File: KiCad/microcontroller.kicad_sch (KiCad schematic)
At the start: 46 parts, among them J1 Debugger, SW1 Reset switch, U1 STM32F051C6Tx, U7 24LC256

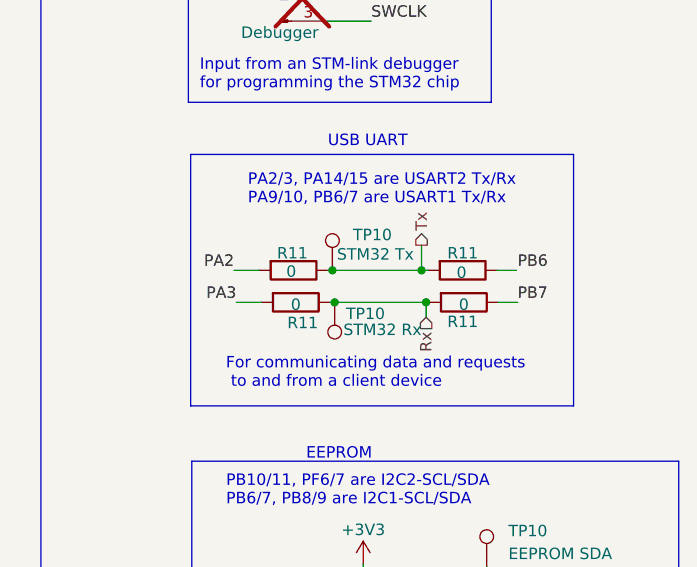
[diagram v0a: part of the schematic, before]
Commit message: updated 0Ω to be DNP
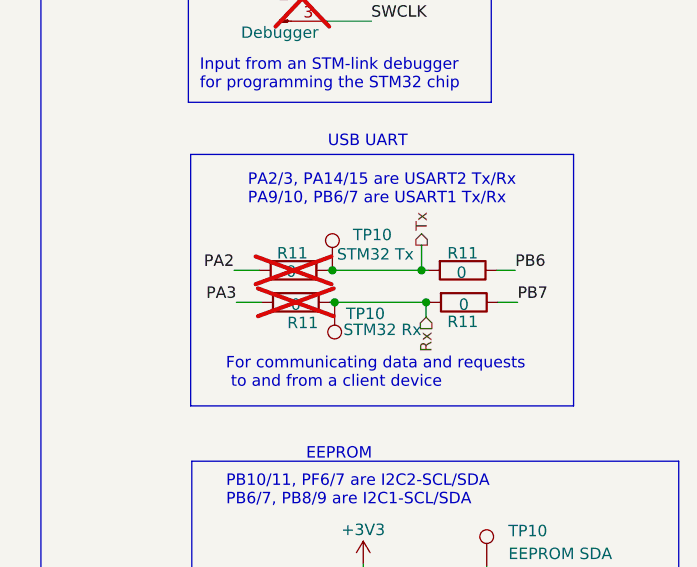
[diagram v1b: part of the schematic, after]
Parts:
- R11: now not fitted
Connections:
- net PB6: now also R11.1
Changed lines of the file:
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@@
-    (stroke (width 0) (type default))
-  )
-  (wire (pts (xy 262.89 64.516) (xy 265.049 64.516))
     (stroke (width 0) (type default))
   )
@@
   )
   (wire (pts (xy 59.69 128.778) (xy 60.96 128.778))
+    (stroke (width 0) (type default))
+  )
+  (wire (pts (xy 262.89 64.516) (xy 264.922 64.516))
     (stroke (width 0) (type default))
   )
@@
     (effects (font (size 1.27 1.27)) (justify left bottom))
   )
-  (label "PB6" (at 265.176 64.516 0) (fields_autoplaced)
+  (label "PB6" (at 264.922 64.516 0) (fields_autoplaced)
     (effects (font (size 1.27 1.27)) (justify left bottom))
   )
@@
   )
   (symbol (lib_id "Device:R") (at 240.284 64.516 270) (unit 1)
-    (in_bom yes) (on_board yes) (dnp no)
+    (in_bom yes) (on_board yes) (dnp yes)
     (property "Reference" "R11" (at 240.157 62.611 90)
       (effects (font (size 1.27 1.27)))
@@
   )
   (symbol (lib_id "Device:R") (at 240.538 68.072 270) (unit 1)
-    (in_bom yes) (on_board yes) (dnp no)
+    (in_bom yes) (on_board yes) (dnp yes)
     (property "Reference" "R11" (at 241.3 70.358 90)
       (effects (font (size 1.27 1.27)))

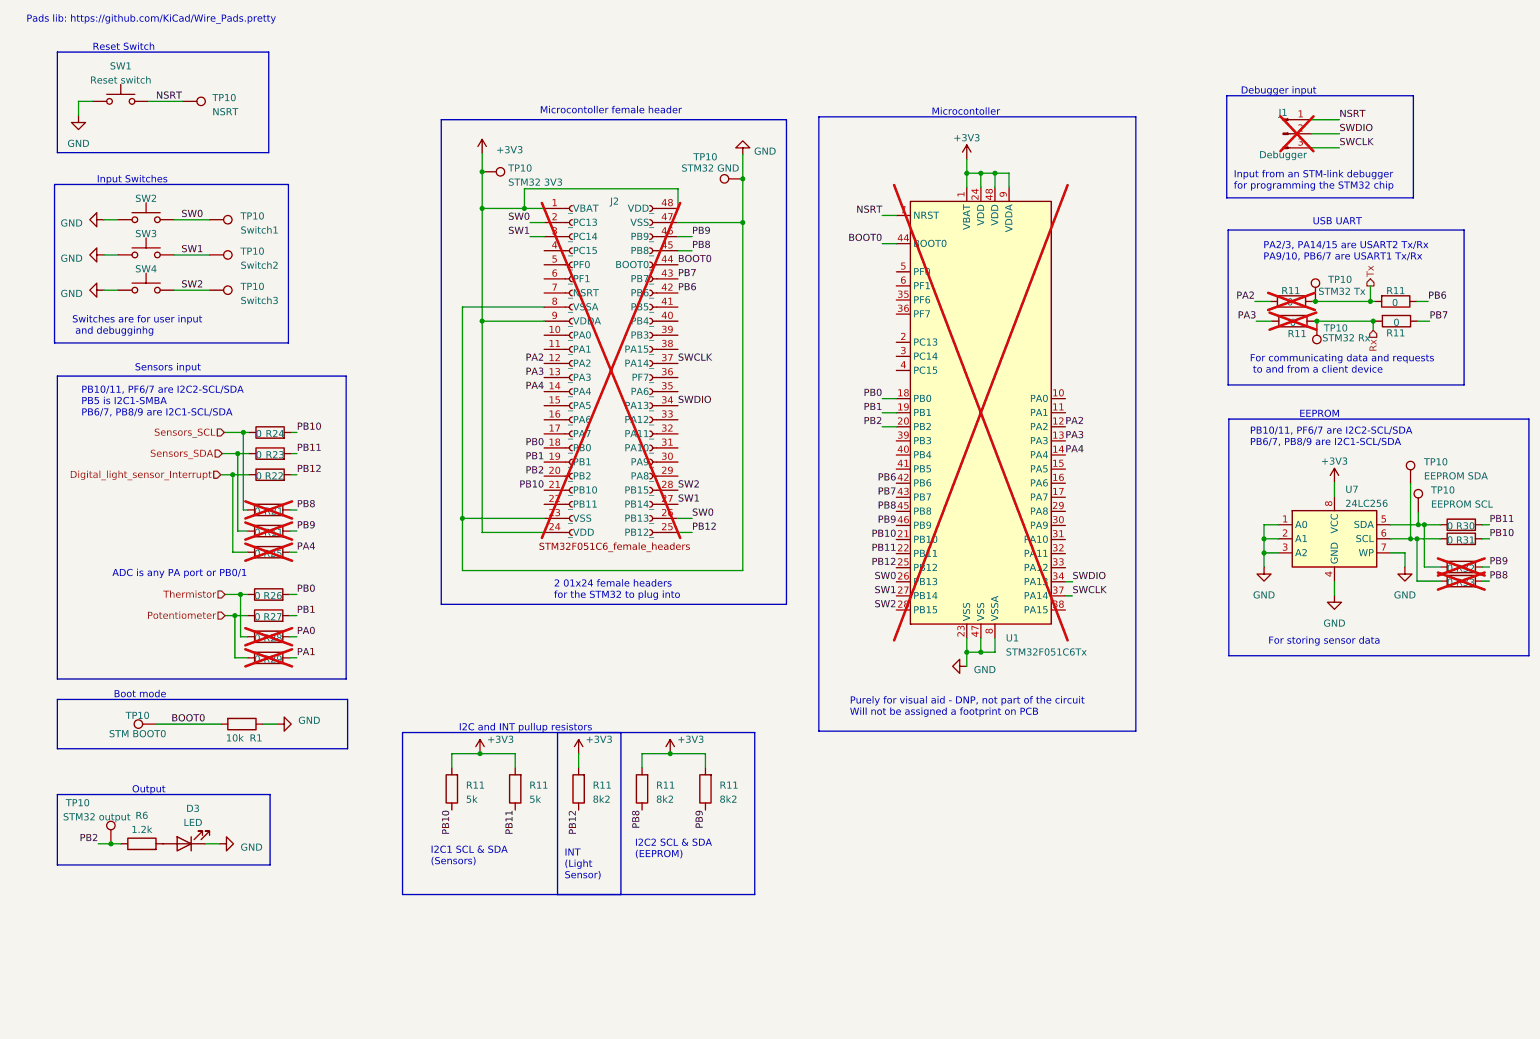
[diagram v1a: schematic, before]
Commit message: changed a bunch of net labels, changed some uc schem stuff
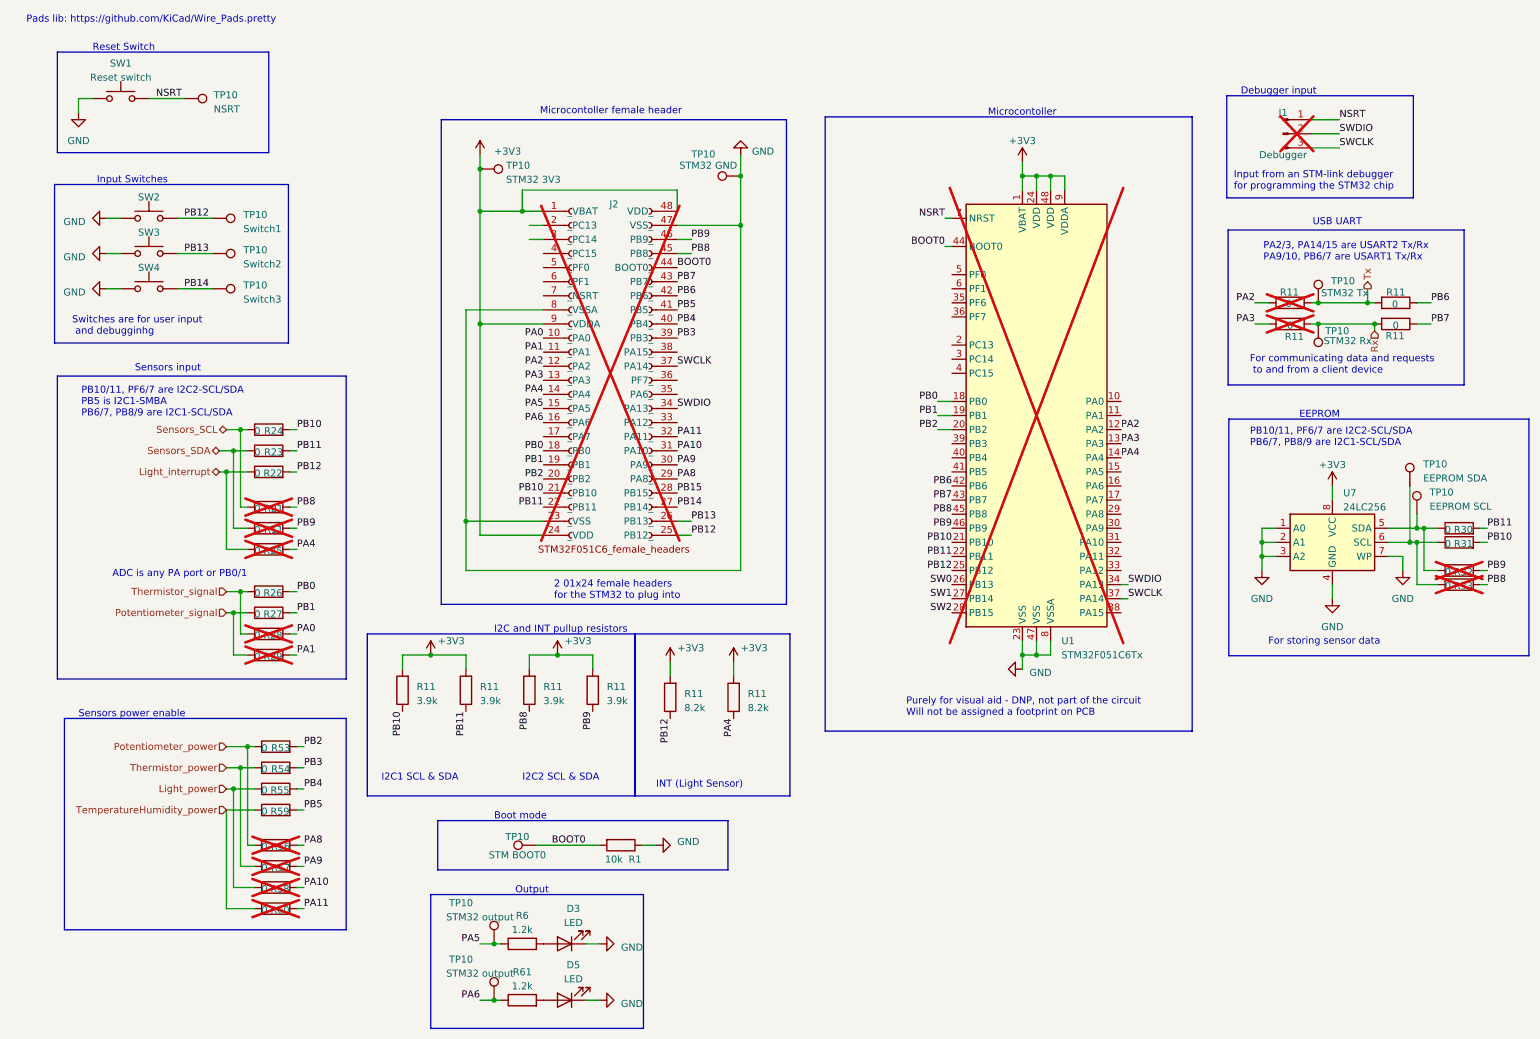
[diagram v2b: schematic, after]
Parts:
- added D5: LED, symbol Device:LED
- added R11: 8.2k, symbol Device:R
- added R53, R54, R55, R56, R57, R58, R59, R60: 0, symbol Device:R
- added R61: 1.2k, symbol Device:R
- added TP10: STM32 output, symbol Connector:TestPoint
- R11: value 5k -> 3.9k
- R11: value 8k2 -> 3.9k
- R11: value 8k2 -> 8.2k
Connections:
- net +3V3: now also R11.2
- net GND: now also D5.1 (K)
- net PA0: now also J2.10 (_PA0)
- net PA1: now also J2.11 (_PA1)
- net PA4: now also R11.1
- net PB11: now also J2.22 (_PB11)
- net PB12: now also SW2.2, TP10.1
- net PB2: now also R53.2; no longer R6.1, TP10.1
- net SW0: no longer J2.2 (_PC13), J2.26 (PB13_), SW2.2, TP10.1
- net SW1: no longer J2.27 (PB14_), J2.3 (_PC14), SW3.2, TP10.1
- net SW2: no longer J2.28 (PB15_), SW4.2, TP10.1
- net PA5: now reaches J2.15 (_PA5)
- net PA5: now also R6.1, TP10.1
- net PA6: now reaches J2.16 (_PA6)
- net PA6: now also R61.1, TP10.1
- net PA8: now reaches J2.29 (PA8_)
- net PA8: now also R56.2
- net PA9: now reaches J2.30 (PA9_)
- net PA9: now also R57.2
- net PA10: now reaches J2.31 (PA10_)
- net PA10: now also R58.2
- net PA11: now reaches J2.32 (PA11_)
- net PA11: now also R60.2
- net PB3: now reaches J2.39 (PB3_)
- net PB3: now also R54.2
- net PB4: now reaches J2.40 (PB4_)
- net PB4: now also R55.2
- net PB5: now reaches J2.41 (PB5_)
- net PB5: now also R59.2
- net Digital_light_sensor_Interrupt renamed Light_interrupt
- net Potentiometer renamed Potentiometer_signal
- net Thermistor renamed Thermistor_signal
- new net: D5.2 (A), R61.2
- new net Light_power: R55.1, R58.1
- new net PB13: J2.26 (PB13_), SW3.2, TP10.1
- new net PB14: J2.27 (PB14_), SW4.2, TP10.1
- new net PB15: J2.28 (PB15_)
- new net Potentiometer_power: R53.1, R56.1
- new net TemperatureHumidity_power: R59.1, R60.1
- new net Thermistor_power: R54.1, R57.1
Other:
- note added: "I2C1 SCL & SDA"
- note added: "I2C2 SCL & SDA"
- note added: "Sensors power enable"
- note removed: "I2C1 SCL & SDA (Sensors)"
- note removed: "I2C2 SCL & SDA (EEPROM)"
- moved on the sheet: D3, J2, R1, R11, R21, R22, R23, R24, R25, R26, R27, R28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

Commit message: updated net labelling scheme on schematic, changed some port connections on microcontroller
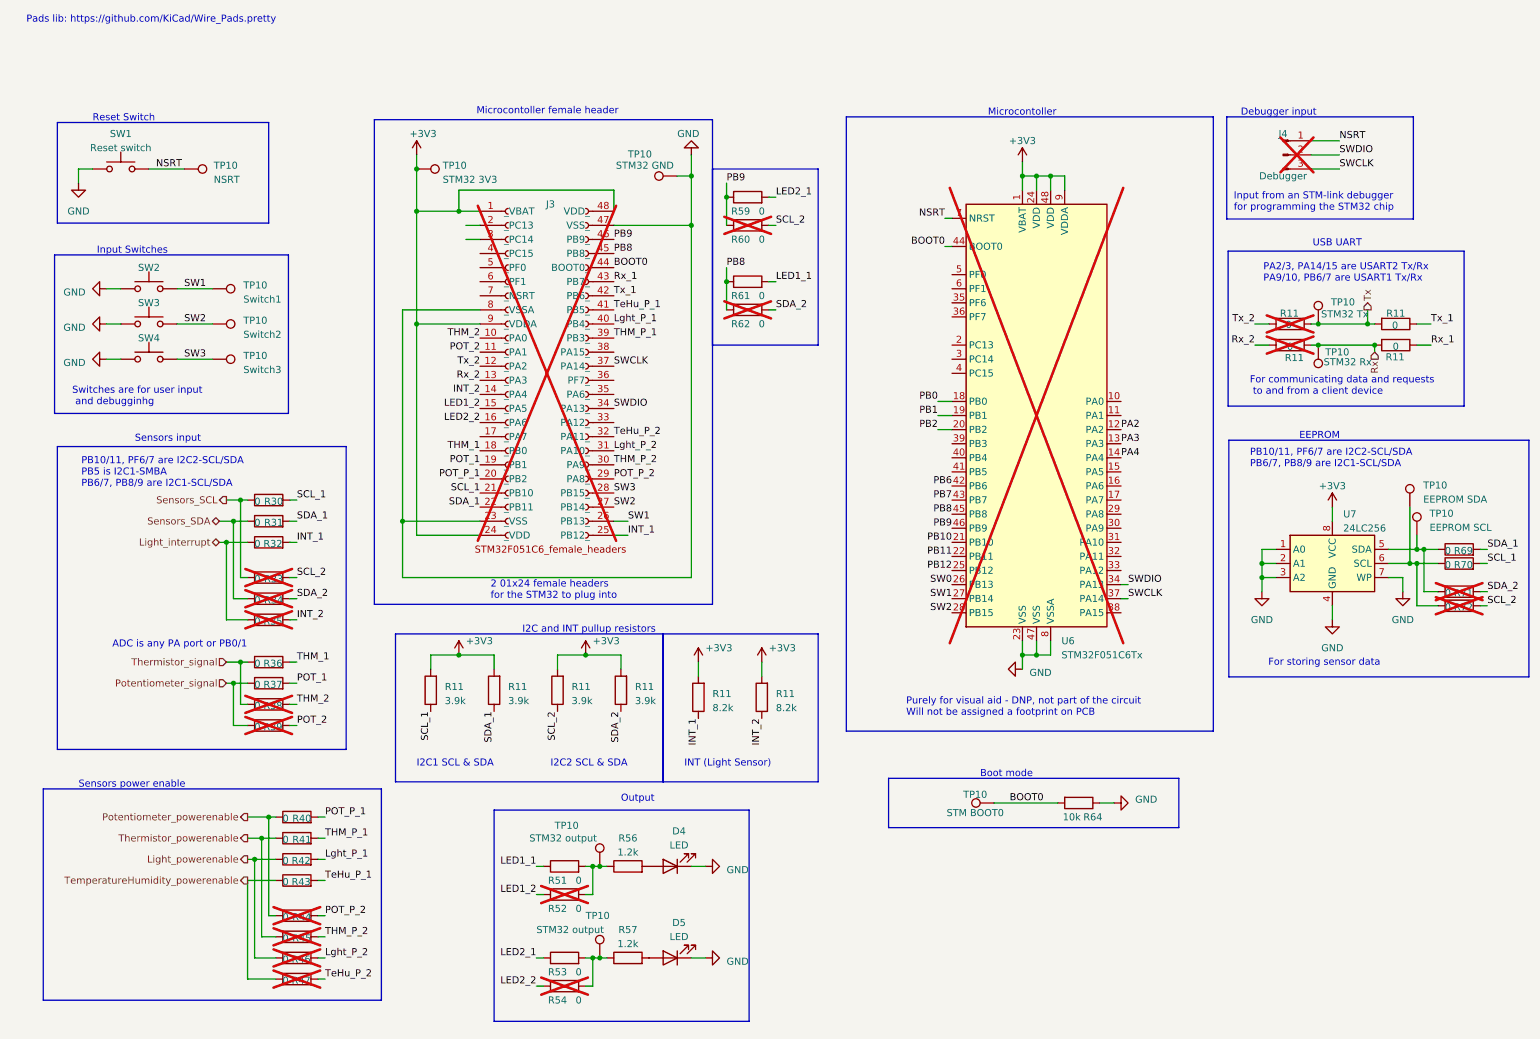
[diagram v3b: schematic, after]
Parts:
- added R51, R52, R53, R54, R59, R60, R61, R62: 0, symbol Device:R
- renumbered D3 to D4, J2 to J3, J1 to J4, R24 to R30, R23 to R31, R22 to R32, R21 to R33, R11 to R34, R25 to R35, R26 to R36, R27 to R37, R28 to R38, R29 to R39, R53 to R40, R54 to R41, R55 to R42, R59 to R43, R56 to R44, R57 to R45, R58 to R46, R60 to R47, R6 to R56, R61 to R57, R1 to R64, R30 to R69, R31 to R70, R32 to R71, R33 to R72, U1 to U6
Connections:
- net PB15 is gone; now on net SW3: J3.28 (PB15_)
- net PA2: no longer J3.12 (_PA2), R11.2
- net PA3: no longer J3.13 (_PA3), R11.2
- net PA4: no longer J3.14 (_PA4), R11.1, R35.2
- net PB0: no longer J3.18 (_PB0), R36.2
- net PB1: no longer J3.19 (_PB1), R37.2
- net PB10: no longer J3.21 (_PB10), R11.1, R30.2, R70.2
- net PB11: no longer J3.22 (_PB11), R11.1, R31.2, R69.2
- net PB12: no longer J3.25 (PB12_), R11.1, R32.2, SW2.2, TP10.1
- net PB2: no longer J3.20 (_PB2), R40.2
- net PB6: no longer J3.42 (PB6_), R11.1
- net PB7: no longer J3.43 (PB7_), R11.1
- net PB8: now also R61.1, R62.1; no longer R11.1, R33.2, R72.2
- net PB9: now also R59.1, R60.1; no longer R11.1, R34.2, R71.2
- net SW1: now also J3.26 (PB13_), SW2.2, TP10.1
- net SW2: now also J3.27 (PB14_), SW3.2, TP10.1
- net Light_power renamed Light_powerenable
- net PA0 renamed THM_2
- net PA1 renamed POT_2
- net PA10 renamed Lght_P_2
- net PA11 renamed TeHu_P_2
- net PA5: no longer names the net of R56.1, TP10.1
- net PA5: now also R51.2, R52.2; no longer J3.15 (_PA5)
- net PA6: no longer names the net of R57.1, TP10.1
- net PA6: now also R53.2, R54.2; no longer J3.16 (_PA6)
- net PA8 renamed POT_P_2
- net PA9 renamed THM_P_2
- removed net PB13: J3.26 (PB13_), SW3.2, TP10.1
- net PB14 renamed SW3
- net SW3: no longer J3.27 (PB14_)
- net PB3 renamed THM_P_1
- net PB4 renamed Lght_P_1
- net PB5 renamed TeHu_P_1
- net Potentiometer_power renamed Potentiometer_powerenable
- net TemperatureHumidity_power renamed TemperatureHumidity_powerenable
- net Thermistor_power renamed Thermistor_powerenable
- new net INT_1: J3.25 (PB12_), R11.1, R32.2
- new net INT_2: J3.14 (_PA4), R11.1, R35.2
- new net LED1_1: R51.1, R61.2
- new net LED1_2: J3.15 (_PA5), R52.1
- new net LED2_1: R53.1, R59.2
- new net LED2_2: J3.16 (_PA6), R54.1
- new net POT_1: J3.19 (_PB1), R37.2
- new net POT_P_1: J3.20 (_PB2), R40.2
- new net Rx_1: J3.43 (PB7_), R11.1
- new net Rx_2: J3.13 (_PA3), R11.2
- new net SCL_1: J3.21 (_PB10), R11.1, R30.2, R70.2
- new net SCL_2: R11.1, R33.2, R60.2, R72.2
- new net SDA_1: J3.22 (_PB11), R11.1, R31.2, R69.2
- new net SDA_2: R11.1, R34.2, R62.2, R71.2
- new net THM_1: J3.18 (_PB0), R36.2
- new net Tx_1: J3.42 (PB6_), R11.1
- new net Tx_2: J3.12 (_PA2), R11.2
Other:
- moved on the sheet: D4, D5, J3, J4, R11, R30, R31, R32, R33, R34, R35, R36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

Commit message: ran ERCs and fixed the errors
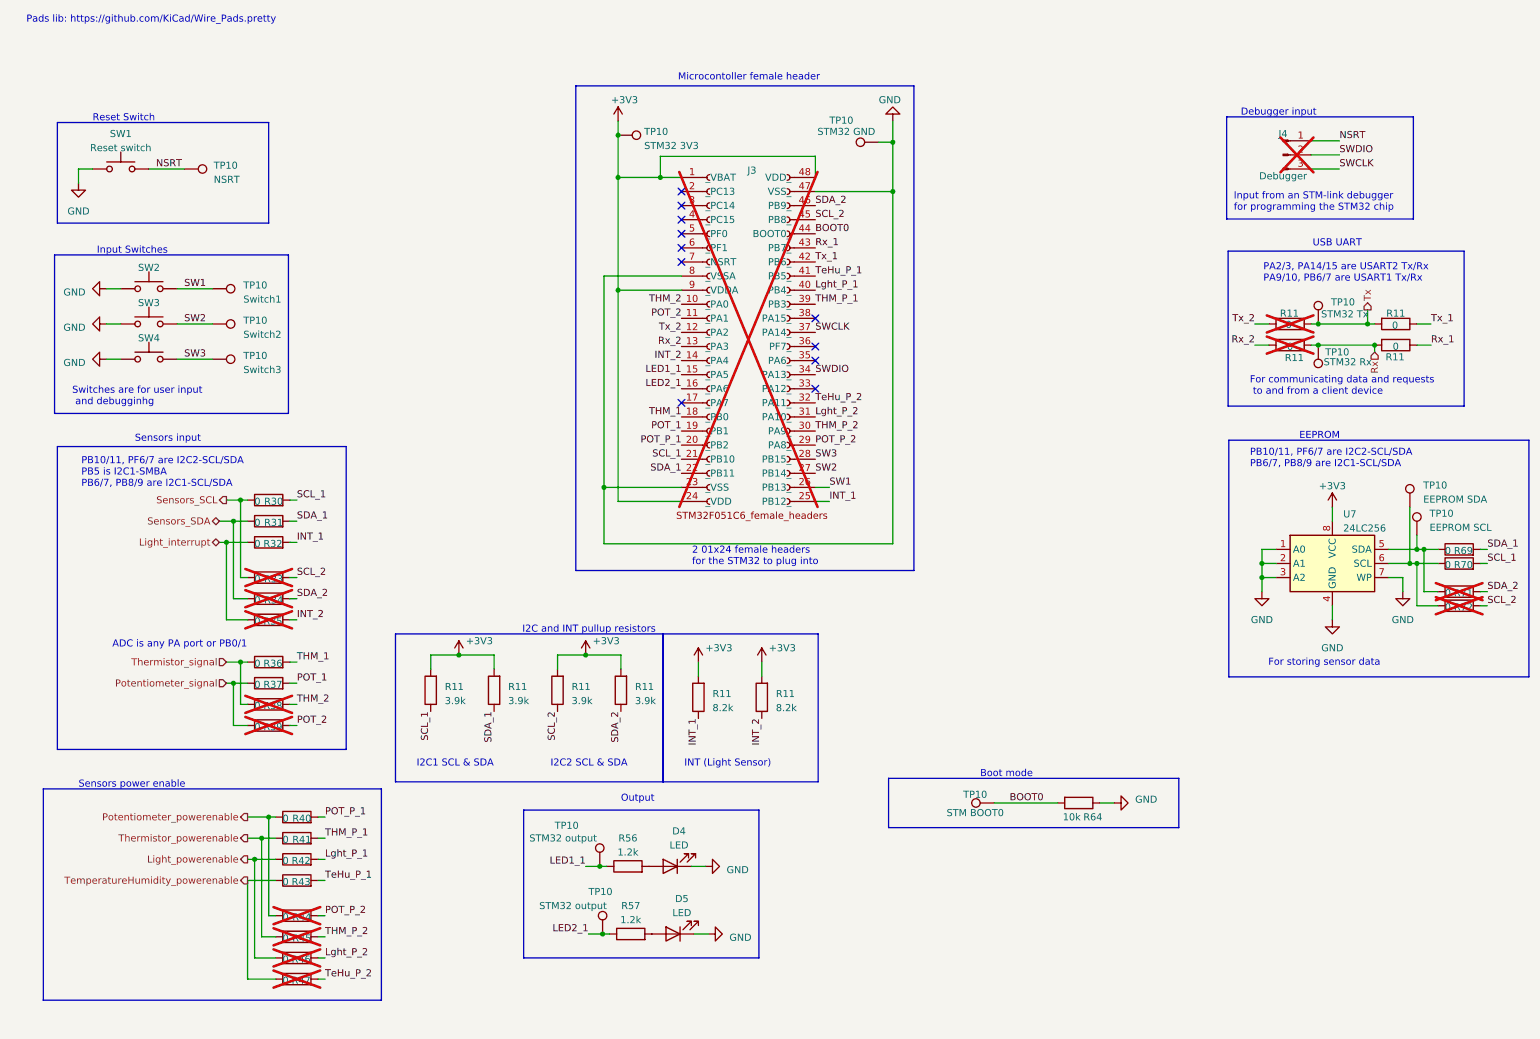
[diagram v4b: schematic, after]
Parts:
- removed R51, R52, R53, R54, R59, R60, R61, R62: 0, symbol Device:R
- removed U6: STM32F051C6Tx, Package_QFP:LQFP-48_7x7mm_P0.5mm, symbol MCU_ST_STM32F0:STM32F051C6Tx
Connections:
- net LED1_2 is gone; now on net LED1_1: J3.15 (_PA5)
- net LED2_2 is gone; now on net LED2_1: J3.16 (_PA6)
- net PB8 is gone; now on net SCL_2: J3.45 (PB8_)
- net PB9 is gone; now on net SDA_2: J3.46 (PB9_)
- net LED1_1: now also R56.1, TP10.1
- net LED2_1: now also R57.1, TP10.1
- no-connect marks 0 -> 11
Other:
- note removed: "Microcontoller"
- note removed: "Purely for visual aid - DNP, not part of the circuit Will not be assigned a footprint on PCB"
- moved on the sheet: D5, J3, R57, TP10

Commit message: bom updated and test labes renamed
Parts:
- D4, D5: Extended Part Cost (none) -> 0; JLC code (none) -> C2286; Part name (none) -> LED_0603; cost per unit (none) -> 0,0054
- J3: Extended Part Cost (none) -> 0; JLC code (none) -> C2883741; Part name (none) -> X6511FV-24-C85D32; cost per unit (none) -> 0
- J4: Extended Part Cost (none) -> 0; JLC code (none) -> C2886705; Part name (none) -> CS-1165SDIG-1*3; cost per unit (none) -> 0
- R11: Extended Part Cost (none) -> 0; JLC code (none) -> C51721; Part name (none) -> 0402WGF3901TCE; cost per unit (none) -> 0,0006
- R11, R30, R31, R32, R33, R34, R35, R36, R37, R38, R39, R40, R41, R42, R43, R44, R45, R46, R47, R69, R70, R71, R72: Extended Part Cost (none) -> 0; JLC code (none) -> C21189; Part name (none) -> 0603WAF0000T5E
- R11: Extended Part Cost (none) -> 0; JLC code (none) -> C25924; Part name (none) -> 0402WGF8201TCE; cost per unit (none) -> 0,0005
- R56, R57, R64: Extended Part Cost (none) -> 0
- SW1, SW2, SW3, SW4: Extended Part Cost (none) -> 0; JLC code (none) -> C318884; Part name (none) -> TS-1187A-B-A-B; cost per unit (none) -> 0,0152
- TP10: Extended Part Cost (none) -> 0; cost per unit (none) -> 0
- U7: Extended Part Cost (none) -> 3; JLC code (none) -> C411624; Part name (none) -> 24LC256; cost per unit (none) -> 1.6033
